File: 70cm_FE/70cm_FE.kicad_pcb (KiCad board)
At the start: 2 copper layers, 50 x 70 mm, 150 parts, among them J2 U.FL, J3 U.FL, J4 U.FL, Q1 2SC3356, Q2 2SC3356, Q3 2SC3356, Q4 2N7002, U1 HT7533-1, U2 74HC14, U3 74HC14, U4 LM393, U5 M68710L

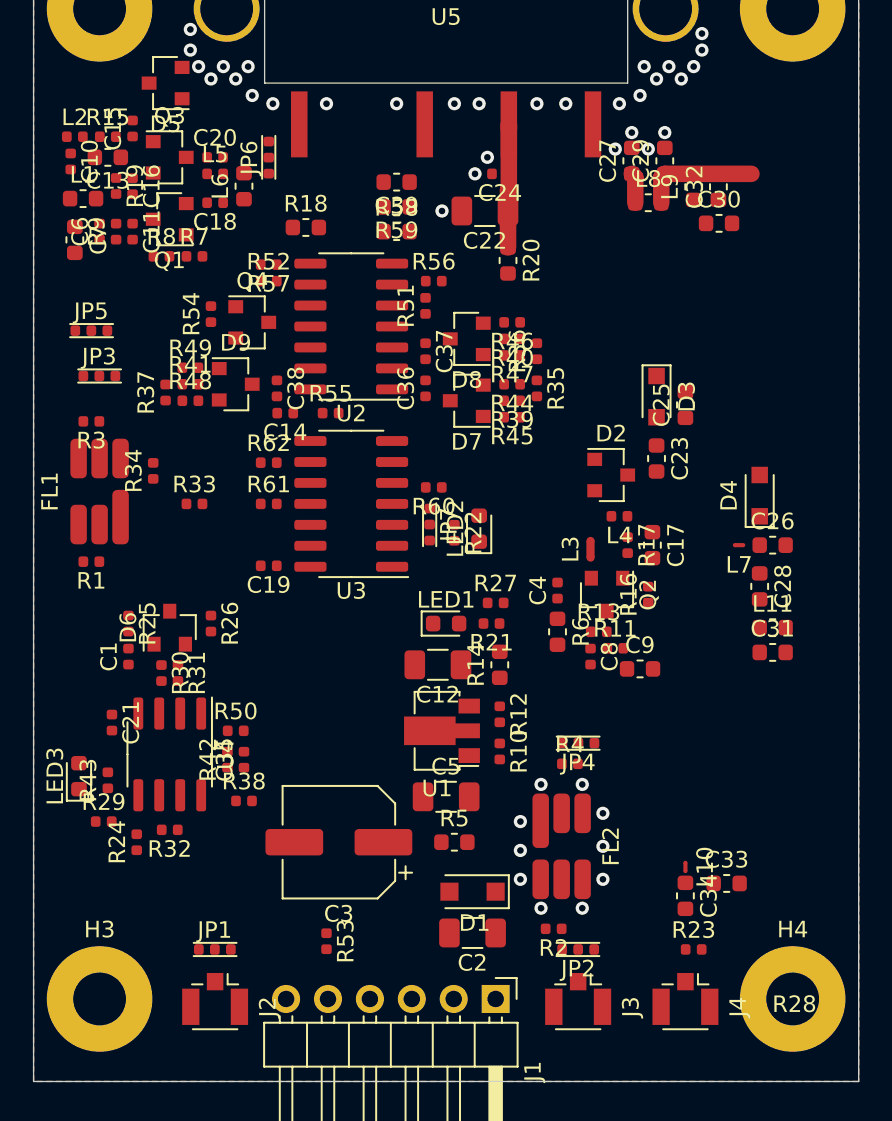
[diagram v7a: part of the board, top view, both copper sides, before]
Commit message: Simplify and improve control circuits, do layout
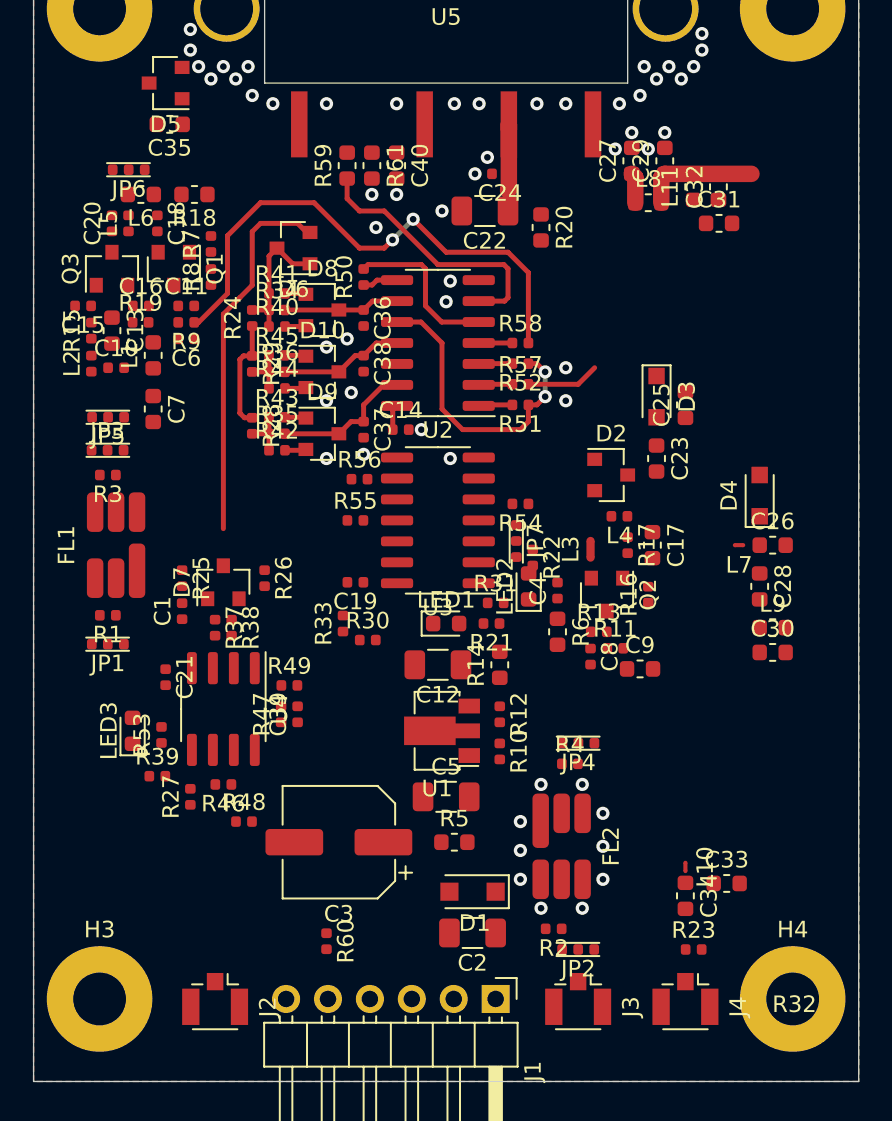
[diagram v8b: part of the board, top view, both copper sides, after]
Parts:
- removed the D7 at (126.2, 78.8)
- removed the D8 at (126.2, 75.0)
- removed Q4: 2N7002, Package_TO_SOT_SMD:SOT-23
- removed the R37 at (108.0, 78.2)
- removed the R39 at (129.0, 78.8)
- removed the R46 at (129.0, 74.0)
- removed the R47 at (129.0, 76.0)
- removed the R48 at (109.5, 78.8)
- removed the R49 at (109.5, 76.8)
- removed the R54 at (110.8, 73.5)
- removed the R55 at (118.0, 79.5)
- added C35: 100p, Capacitor_SMD:C_0603_1608Metric, F.Cu at (108.2, 62.0)
- added D10: BAV99, Package_TO_SOT_SMD:SOT-23, F.Cu at (117.5, 77.0)
- added D6: BAV99, Package_TO_SOT_SMD:SOT-23, F.Cu at (115.8, 69.5)
- added D9: BAV99, Package_TO_SOT_SMD:SOT-23, F.Cu at (117.5, 80.8)
- added R24: 1k, Resistor_SMD:R_0402_1005Metric, F.Cu at (113.2, 73.7)
- added R28: 1k, Resistor_SMD:R_0402_1005Metric, F.Cu at (113.2, 80.3)
- added R29: 1k, Resistor_SMD:R_0402_1005Metric, F.Cu at (113.2, 76.5)
- added R34: 100k, Resistor_SMD:R_0402_1005Metric, F.Cu at (114.8, 73.2)
- added R42: DNP, Resistor_SMD:R_0402_1005Metric, F.Cu at (114.8, 81.8)
- added R43: 0, Resistor_SMD:R_0402_1005Metric, F.Cu at (114.8, 79.8)
- added R50: 0, Resistor_SMD:R_0402_1005Metric, F.Cu at (120.0, 71.2)
- R35: value 0 -> 220k
- R36: value 0 -> 100k
- R40: value 100k -> 100
- R41, R45: value 0 -> DNP
- moved JP1 19.3 mm to (105.0, 93.5), turned to 180 degrees
- moved R52 16.0 mm to (129.5, 76.5), turned to 180 degrees
- moved R35 16.0 mm to (114.8, 80.8), turned to 0 degrees
- moved R58 16.0 mm to (129.5, 75.2), turned to 0 degrees
- moved R36 15.8 mm to (114.8, 77.0), turned to 0 degrees
- moved R33 14.8 mm to (118.8, 92.2)
- moved R45 14.7 mm to (114.8, 76.0), turned to 0 degrees
- moved R40 14.3 mm to (114.8, 74.2), turned to 0 degrees
- moved R44 14.3 mm to (114.8, 78.0), turned to 0 degrees
- moved L2 13.8 mm to (103.5, 76.5), turned to 90 degrees
- moved R30 13.4 mm to (120.2, 93.2)
- moved C10 12.8 mm to (105.0, 76.8), turned to 0 degrees
- moved R15 11.8 mm to (103.5, 74.5), turned to 90 degrees
- moved C7 11.3 mm to (107.2, 79.2)
- moved C15 11.2 mm to (103.0, 73.0), turned to 180 degrees
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- renumbered C31 to C30, C30 to C31, C35 to C39, C39 to C40, D6 to D7, D9 to D8, L9 to L11, L11 to L9, R24 to R27, R33 to R30, R27 to R31, R28 to R32, R34 to R33, R30 to R37, R31 to R38, R29 to R39, R32 to R46, R42 to R47, R38 to R48, R50 to R49, R43 to R53, R60 to R54, R61 to R55, R62 to R56, R56 to R57, R57 to R58, R58 to R59, R53 to R60, R59 to R61
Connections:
- C36 pad 1: /~LNA_SEQ_IN~ -> /PA_SEQ_IN
- C37 pad 1: /PIN_SEQ_IN -> /~LNA_SEQ_IN~
- C38 pad 1: /PA_SEQ_IN -> /PIN_SEQ_IN
- D8 pad 1: Net-(D9-Pad1) -> Net-(D8-Pad1)
- D8 pad 2: Net-(D9-Pad2) -> Net-(D8-Pad2)
- R35 pad 1: /TX_ON -> /~LNA_SEQ_MID~
- R35 pad 2: /~LNA_EN_IN~ -> /~LNA_SEQ_IN~
- R36 pad 1: /TX_ON -> /PIN_SEQ_MID
- R36 pad 2: /~PIN_EN_IN~ -> /PIN_SEQ_IN
- R40 pad 1: /~PIN_EN_IN~ -> /PA_SEQ_MID
- R40 pad 2: /PIN_SEQ_IN -> Net-(D8-Pad2)
- R41 pad 1: /~PA_EN_IN~ -> /PA_SEQ_MID
- R41 pad 2: /PA_SEQ_IN -> Net-(D8-Pad1)
- R44 pad 1: /~LNA_EN_IN~ -> /PIN_SEQ_MID
- R45 pad 1: /~LNA_EN_IN~ -> /PIN_SEQ_MID
- U2 pad 1: /~LNA_SEQ_IN~ -> /~PIN_EN_~
- U2 pad 10: /PA_EN -> /~PIN_SEQ_OUT~
- U2 pad 11: /~PA_EN_~ -> /PIN_SEQ_IN
- U2 pad 12: /~PA_SEQ_OUT~ -> /LNA_EN
- U2 pad 13: /PA_SEQ_IN -> /~LNA_SEQ_IN~
- U2 pad 2: /LNA_EN -> /PIN_EN
- U2 pad 3: /PIN_SEQ_IN -> /~DRV_EN_~
- U2 pad 4: /~PIN_SEQ_OUT~ -> /DRV_EN1
- U2 pad 5: /~PIN_EN_~ -> /~PA_EN_~
- U2 pad 6: /PIN_EN -> /PA_EN
- U2 pad 8: /DRV_EN1 -> /~PA_SEQ_OUT~
- U2 pad 9: /~DRV_EN_~ -> /PA_SEQ_IN
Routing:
- net /DRV_EN: track 0.00 -> 32.8 mm, vias 0 -> 2
- net /~OverTemp~: track 0.00 -> 22.7 mm
- net /~PIN_SEQ_OUT~: track 0.00 -> 18.2 mm, vias 0 -> 2
- net /PA_EN: track 0.00 -> 16.3 mm
- net /~PA_EN_~: track 0.00 -> 9.84 mm
- net /~LNA_SEQ_IN~: track 0.00 -> 8.61 mm
- net /PA_SEQ_MID: track 0.00 -> 8.36 mm
- net /PIN_SEQ_IN: track 0.00 -> 7.51 mm
- net /PA_SEQ_IN: track 0.00 -> 7.01 mm
- net /TX_ON: track 0.00 -> 6.77 mm
- net /PIN_bias: track 0.00 -> 4.43 mm
- net /PA_VDD: track 7.78 -> 4.32 mm
- net /~LNA_SEQ_MID~: track 0.00 -> 3.02 mm
- net /PIN_SEQ_MID: track 0.00 -> 3.02 mm
- net /~PA_SEQ_OUT~: track 0.00 -> 2.15 mm
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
